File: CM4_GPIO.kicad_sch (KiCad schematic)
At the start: 28 parts, among them J1 Conn_01x03, J2 Conn_02x07_Odd_Even, J3 Conn_01x03, J7 Micro_SD_Card_Det, J8 THD-20-R, J9 THD-02-R, U1 TPD4EUSB30, U18 RT9742GGJ5, U2 TPD4EUSB30, U3 MagJack-A70-112-331N126, U5 74LVC1G07SE-7, U9 74LVC1G07SE-7

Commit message: removed HDMI, CAM and DISP1 connectors
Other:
- company: © 2020-2022 Raspberry Pi Ltd (formerly Raspberry Pi (Trading) Ltd.) -> (none)
- title: Compute Module 4 IO Board - GPIO - Ethernet -> Bitcart
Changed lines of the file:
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@@
   (paper "A4")
   (title_block
-    (title "Compute Module 4 IO Board - GPIO - Ethernet")
+    (title "Bitcart")
+    (date "2023-09-15")
     (rev "1")
-    (company "© 2020-2022 Raspberry Pi Ltd (formerly Raspberry Pi (Trading) Ltd.)")
-    (comment 1 "www.raspberrypi.com")
   )
   (junction (at 37.846 92.71) (diameter 1.016) (color 0 0 0 0)

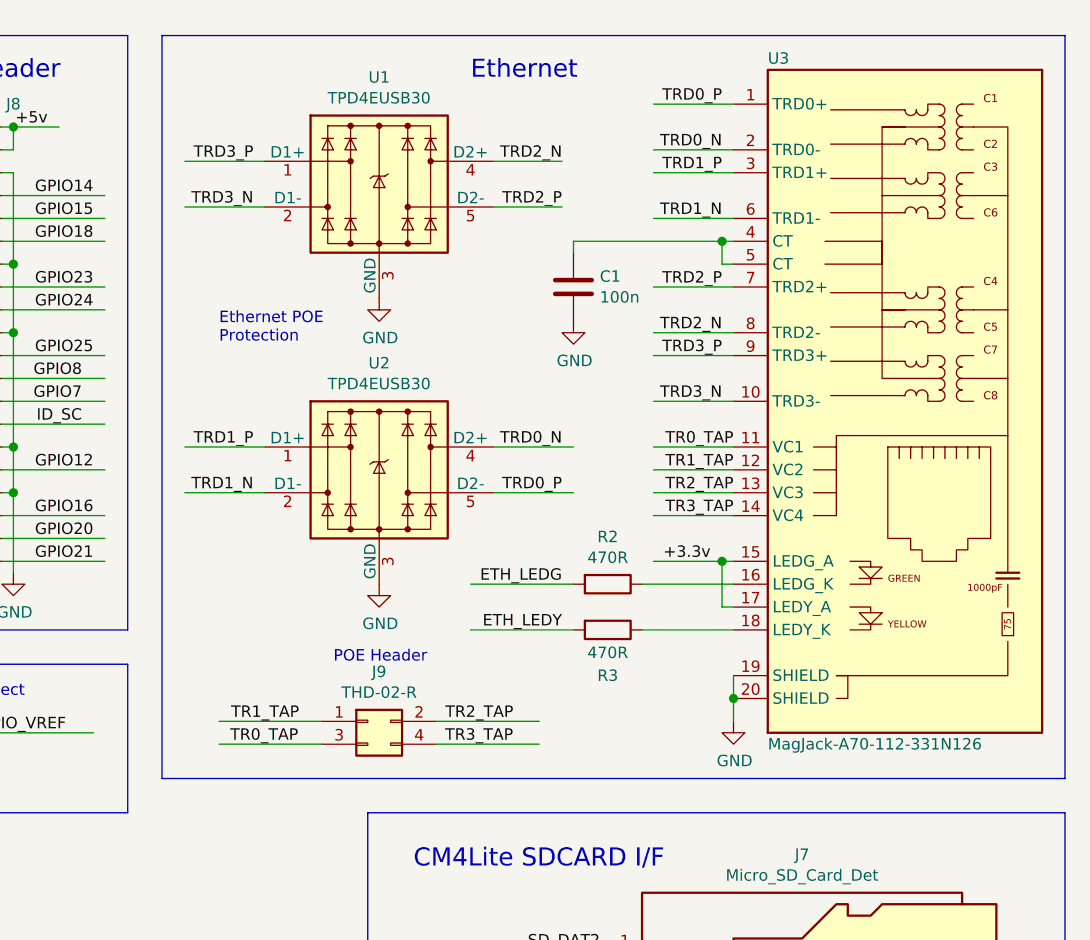
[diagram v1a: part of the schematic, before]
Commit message: added hashboard connectors. added GPU power connector
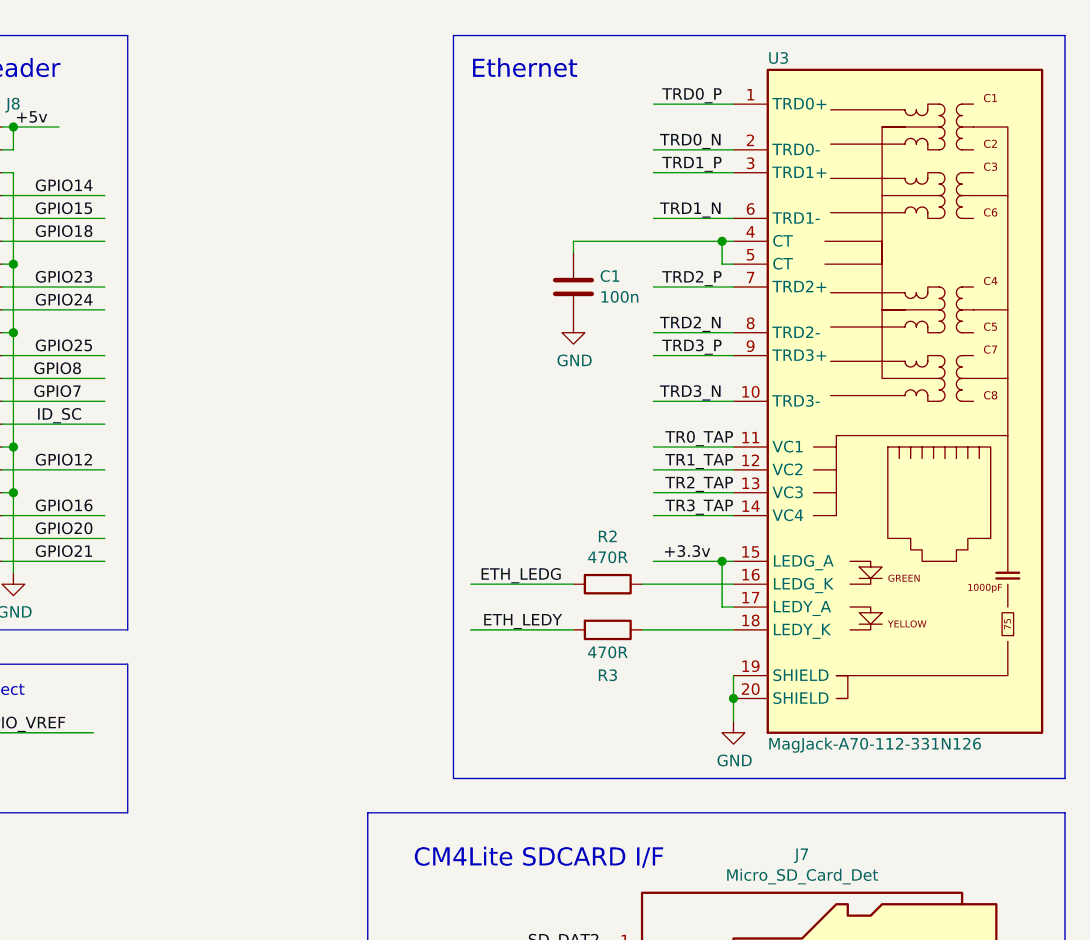
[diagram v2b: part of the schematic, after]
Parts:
- removed J9: THD-02-R, Connector_PinHeader_2.54mm:PinHeader_2x02_P2.54mm_Vertical, symbol Connector_Generic:Conn_02x02_Odd_Even
- removed U1, U2: TPD4EUSB30, Package_SON:USON-10_2.5x1.0mm_P0.5mm, symbol CM4IO:TPD4EUSB30
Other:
- note removed: "Ethernet POE Protection"
- note removed: "POE Header"

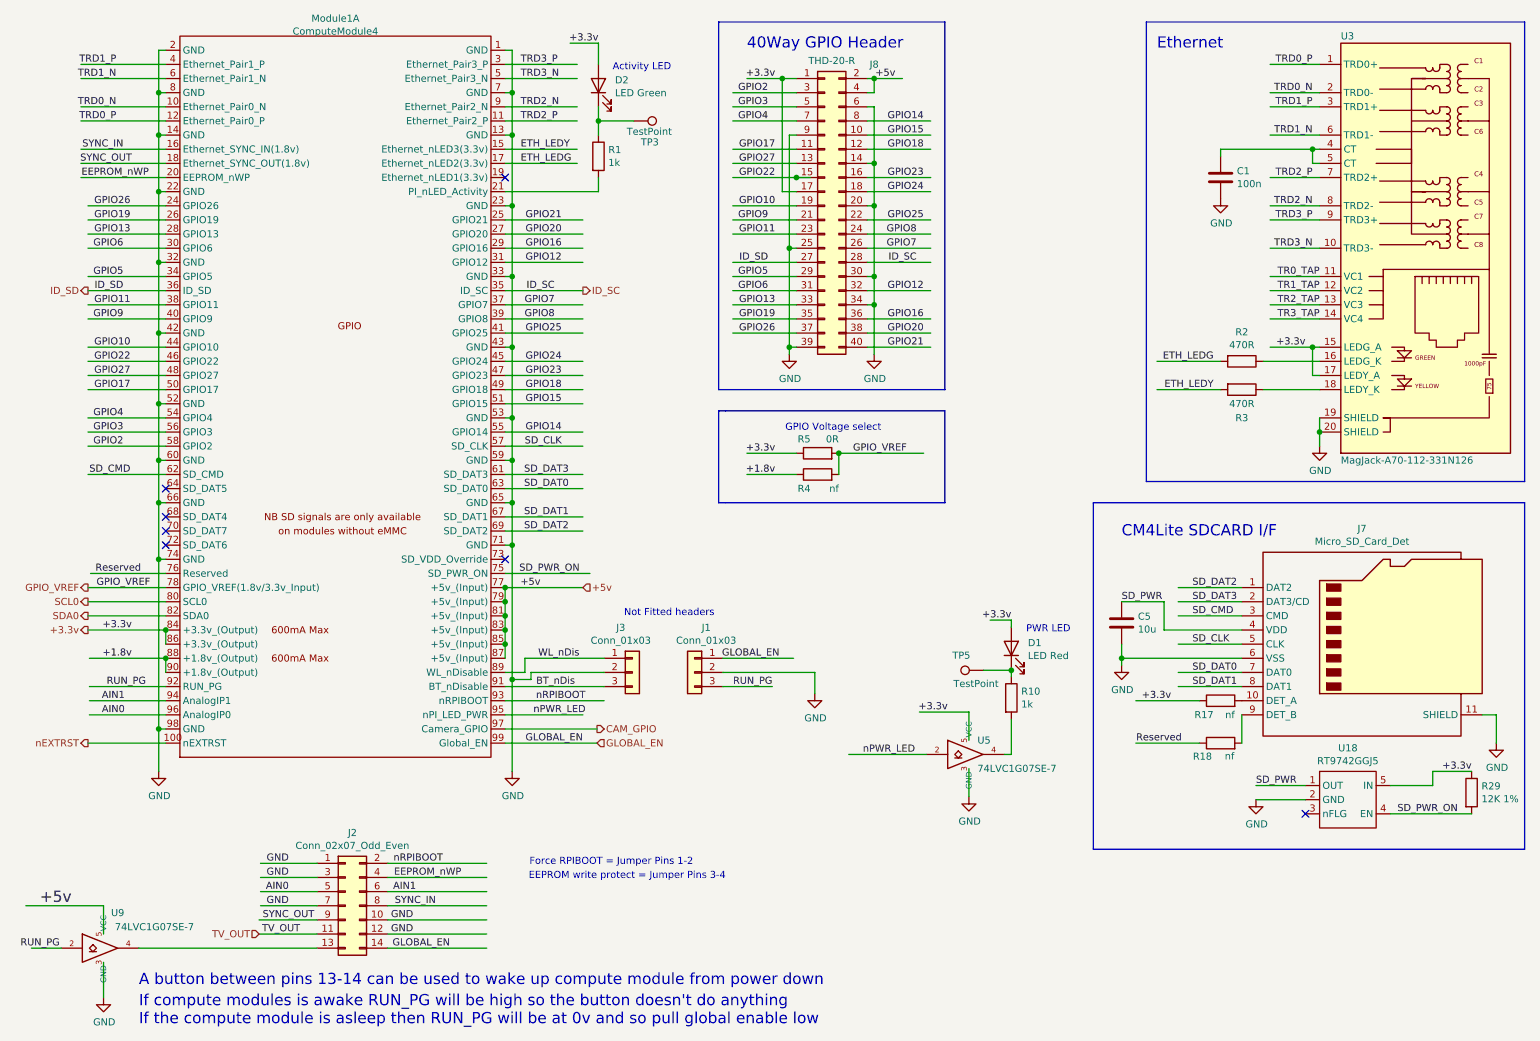
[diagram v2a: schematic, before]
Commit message: extended the board to make room for IO connectors. added the vertical display connector.
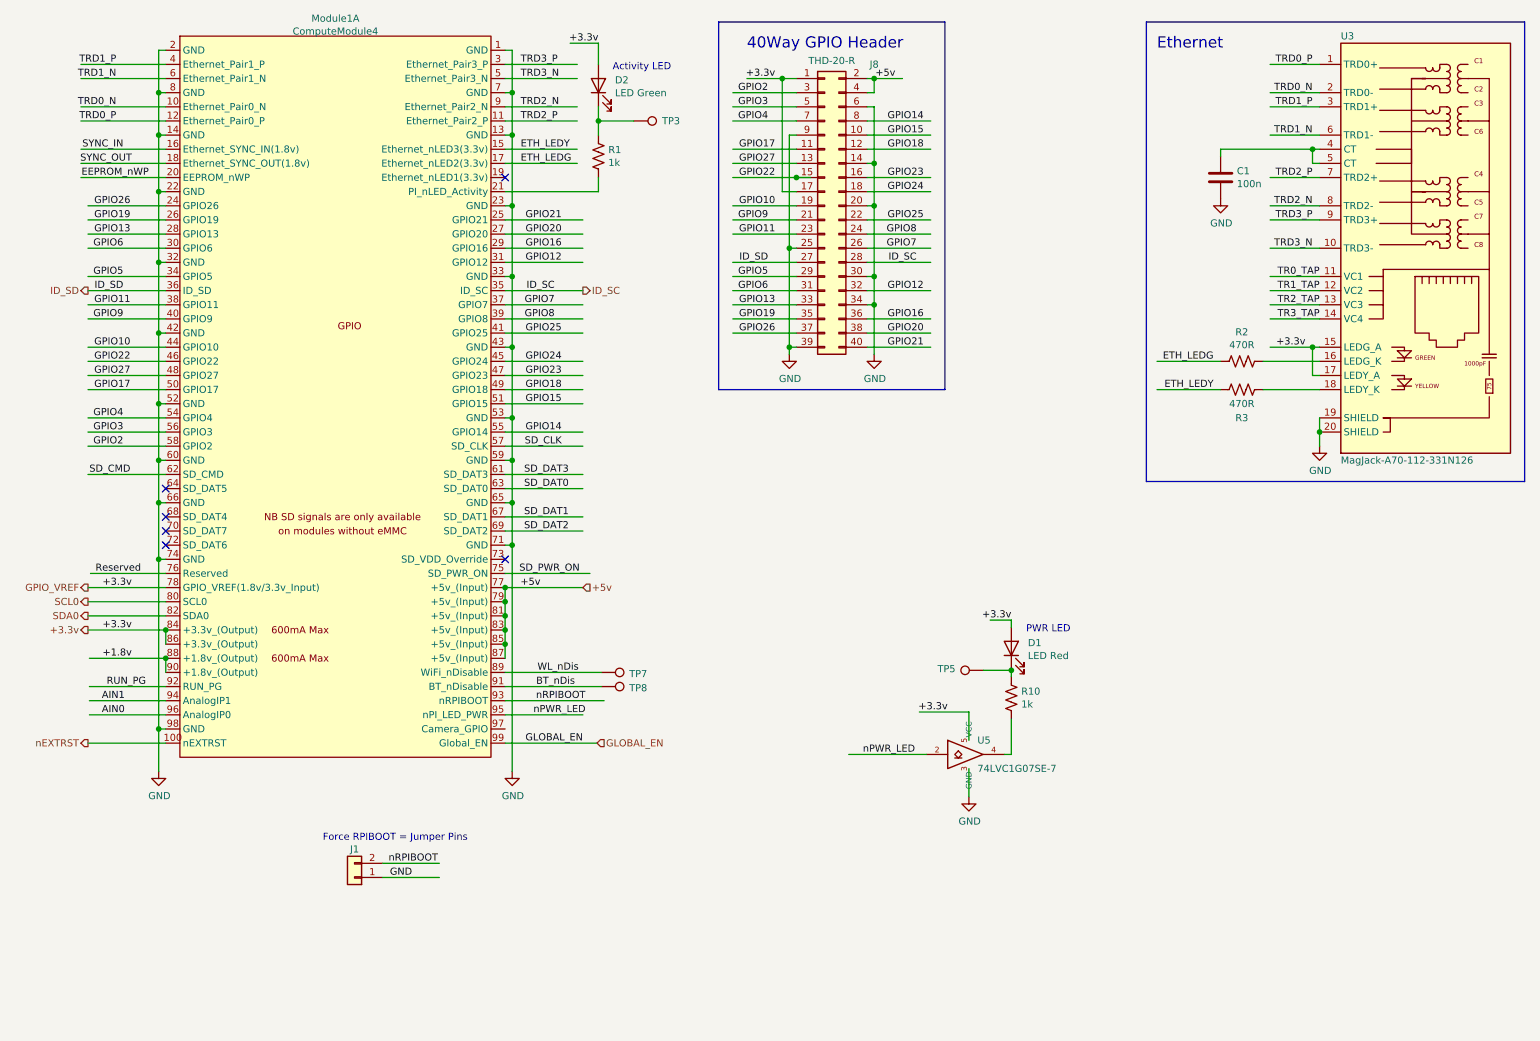
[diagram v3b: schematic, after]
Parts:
- removed C5: 10u, Capacitor_SMD:C_0805_2012Metric, symbol Device:C
- removed J1, J3: Conn_01x03, Connector_PinHeader_2.54mm:PinHeader_1x03_P2.54mm_Vertical, symbol Connector_Generic:Conn_01x03
- removed J2: Conn_02x07_Odd_Even, Connector_PinHeader_2.54mm:PinHeader_2x07_P2.54mm_Vertical, symbol Connector_Generic:Conn_02x07_Odd_Even
- removed J7: Micro_SD_Card_Det, CM4IO:SDCARD_MOLEX_503398-1892, symbol Connector:Micro_SD_Card_Det
- removed R17, R18: nf, Resistor_SMD:R_0402_1005Metric, symbol Device:R
- removed R29: 12K 1%, Resistor_SMD:R_0402_1005Metric, symbol Device:R
- removed R4: nf, Resistor_SMD:R_0805_2012Metric_Pad1.15x1.40mm_HandSolder, symbol Device:R
- removed R5: 0R, Resistor_SMD:R_0805_2012Metric_Pad1.15x1.40mm_HandSolder, symbol Device:R
- removed U18: RT9742GGJ5, Package_TO_SOT_SMD:SOT-23-5, symbol CM4IO:RT9742GGJ5
- removed U9: 74LVC1G07SE-7, Package_TO_SOT_SMD:SOT-353_SC-70-5, symbol CM4IO:74LVC1G07_copy
- added J1: Conn_01x02, Connector_PinHeader_2.54mm:PinHeader_1x02_P2.54mm_Vertical, symbol Connector_Generic:Conn_01x02
- added TP7, TP8: TestPoint, TestPoint:TestPoint_Pad_D1.5mm, symbol Connector:TestPoint
- Module1: Field5 2off DF40C-100DS-0.4V -> 2x DF40C-100DS-0.4V
- R1, R10, R2, R3: symbol Device:R -> Device:R_US
- TP3, TP5: footprint TestPoint:TestPoint_Pad_2.0x2.0mm -> TestPoint:TestPoint_Pad_D1.5mm
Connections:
- net GPIO_VREF is gone; now on net +3.3v: Module1.78 (GPIO_VREF(1.8v/3.3v_Input))
- net BT_nDis: now also TP8.1
- net GND: now also J1.1 (Pin_1)
- net WL_nDis: now also TP7.1
- net nRPIBOOT: now also J1.2 (Pin_2)
- net CAM_GPIO: no longer names the net of Module1.97 (Camera_GPIO)
- no-connect marks 7 -> 6
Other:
- note added: "Force RPIBOOT = Jumper Pins"
- note removed: "A button between pins 13-14 can be used to wake up compute module from power down"
- note removed: "CM4Lite SDCARD I/F"
- note removed: "EEPROM write protect = Jumper Pins 3-4"
- note removed: "Force RPIBOOT = Jumper Pins 1-2"
- note removed: "GPIO Voltage select"
- note removed: "If compute modules is awake RUN_PG will be high so the button doesn't do anything If the compute module is asleep then RUN_PG will be at 0v and so pull global enable low"
- note removed: "Not Fitted headers"

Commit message: added the PSU control connector.
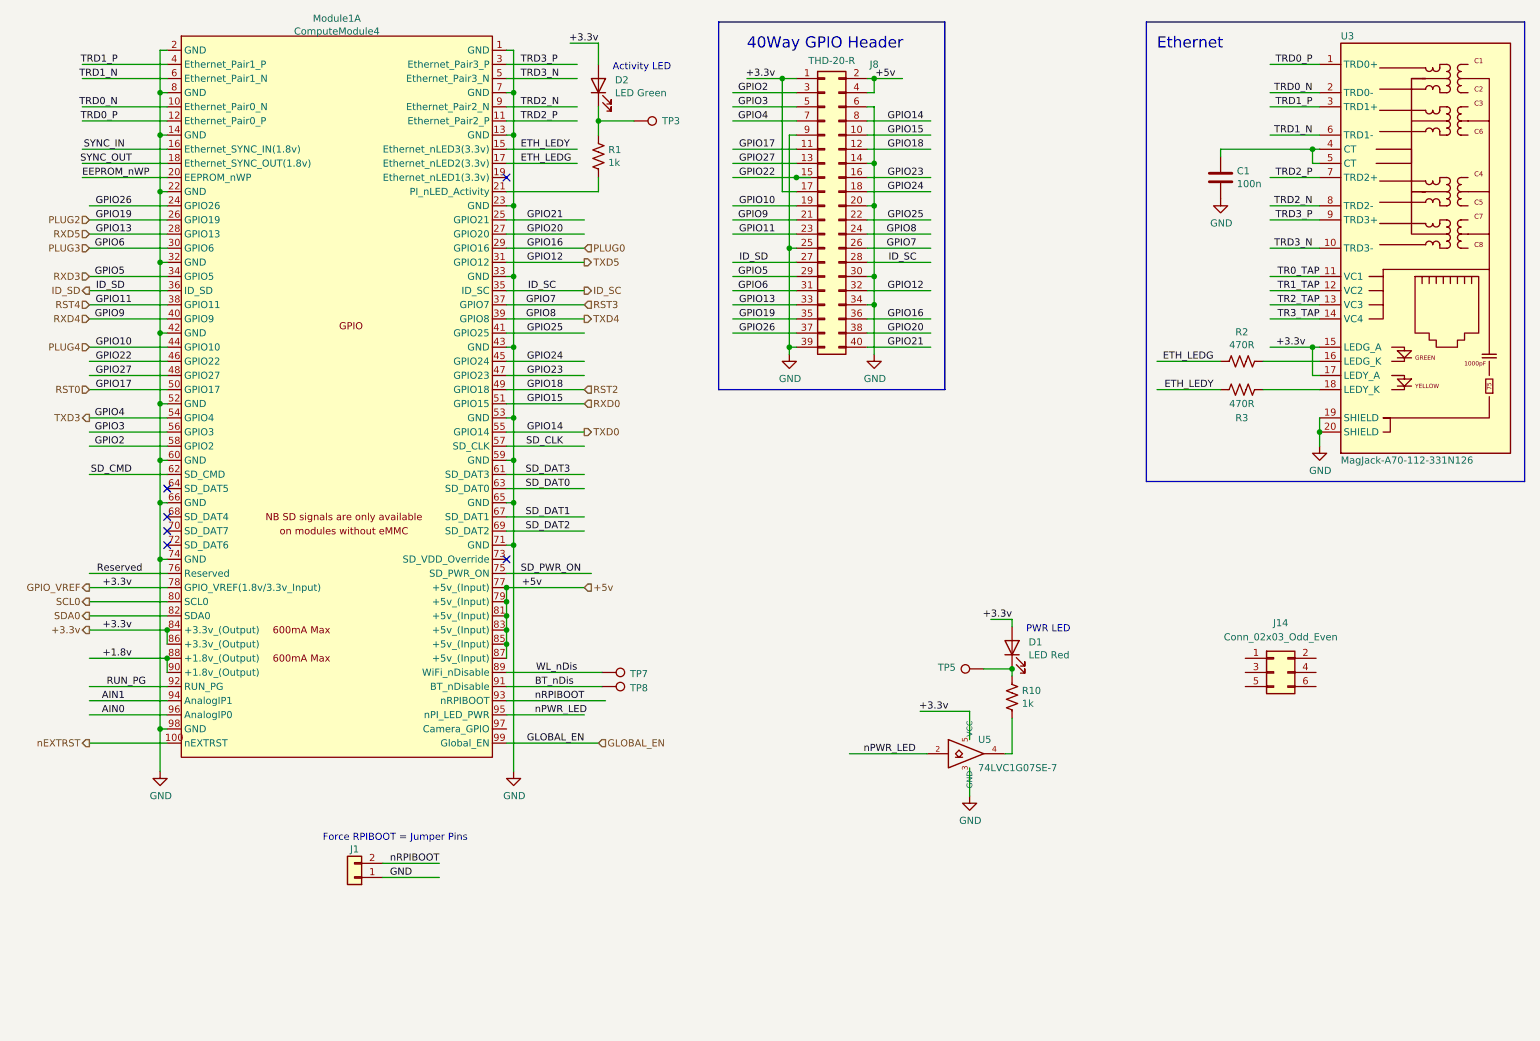
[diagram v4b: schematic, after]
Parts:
- added J14: Conn_02x03_Odd_Even, bitcart:CONN-TH_6P-P2.00_PHD-2X3A, symbol Connector_Generic:Conn_02x03_Odd_Even
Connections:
- net GPIO10 renamed PLUG4
- net GPIO11 renamed RST4
- net GPIO12 renamed TXD5
- net GPIO13 renamed RXD5
- net GPIO14 renamed TXD0
- net GPIO15 renamed RXD0
- net GPIO16 renamed PLUG0
- net GPIO17 renamed RST0
- net GPIO18 renamed RST2
- net GPIO19 renamed PLUG2
- net GPIO4 renamed TXD3
- net GPIO5 renamed RXD3
- net GPIO6 renamed PLUG3
- net GPIO7 renamed RST3
- net GPIO8 renamed TXD4
- net GPIO9 renamed RXD4

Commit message: finding/adding digikey part numbers
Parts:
- Module1: DK (none) -> 26-DF40C-100DS-0.4V(58)CT-ND; Field4 Hirose -> (none); Field5 2x DF40C-100DS-0.4V -> (none); Field6 2off DF40C-100DS-0.4V -> (none); Field7 Hirose -> (none); PARTNO (none) -> DF40C-100DS-0.4V(58); Part Description 100 Position Connector Receptacle, Center Strip Contacts Su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 -> (none)
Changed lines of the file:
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@@
       (effects (font (size 1.27 1.27)) hide)
     )
-    (property "Field4" "Hirose" (at 72.39 74.93 0)
+    (property "DK" "26-DF40C-100DS-0.4V(58)CT-ND" (at 72.39 74.93 0)
       (effects (font (size 1.27 1.27)) hide)
     )
-    (property "Field5" "2x DF40C-100DS-0.4V" (at 72.39 74.93 0)
+    (property "PARTNO" "DF40C-100DS-0.4V(58)" (at 72.39 74.93 0)
       (effects (font (size 1.27 1.27)) hide)
     )
-    (property "Field6" "2off DF40C-100DS-0.4V" (at 72.39 74.93 0)
-      (effects (font (size 1.27 1.27)) hide)
-    )
-    (property "Field7" "Hirose" (at 72.39 74.93 0)
-      (effects (font (size 1.27 1.27)) hide)
-    )
-    (property "Part Description" "	100 Position Connector Receptacle, Center Strip Contacts Surface Mount Gold" (at 72.39 74.93 0)
-      (effects (font (size 1.27 1.27)) hide)
-    )
